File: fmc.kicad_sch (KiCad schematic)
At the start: 2 parts, among them P1 ASP-134604-01, P2 ASP-134604-01

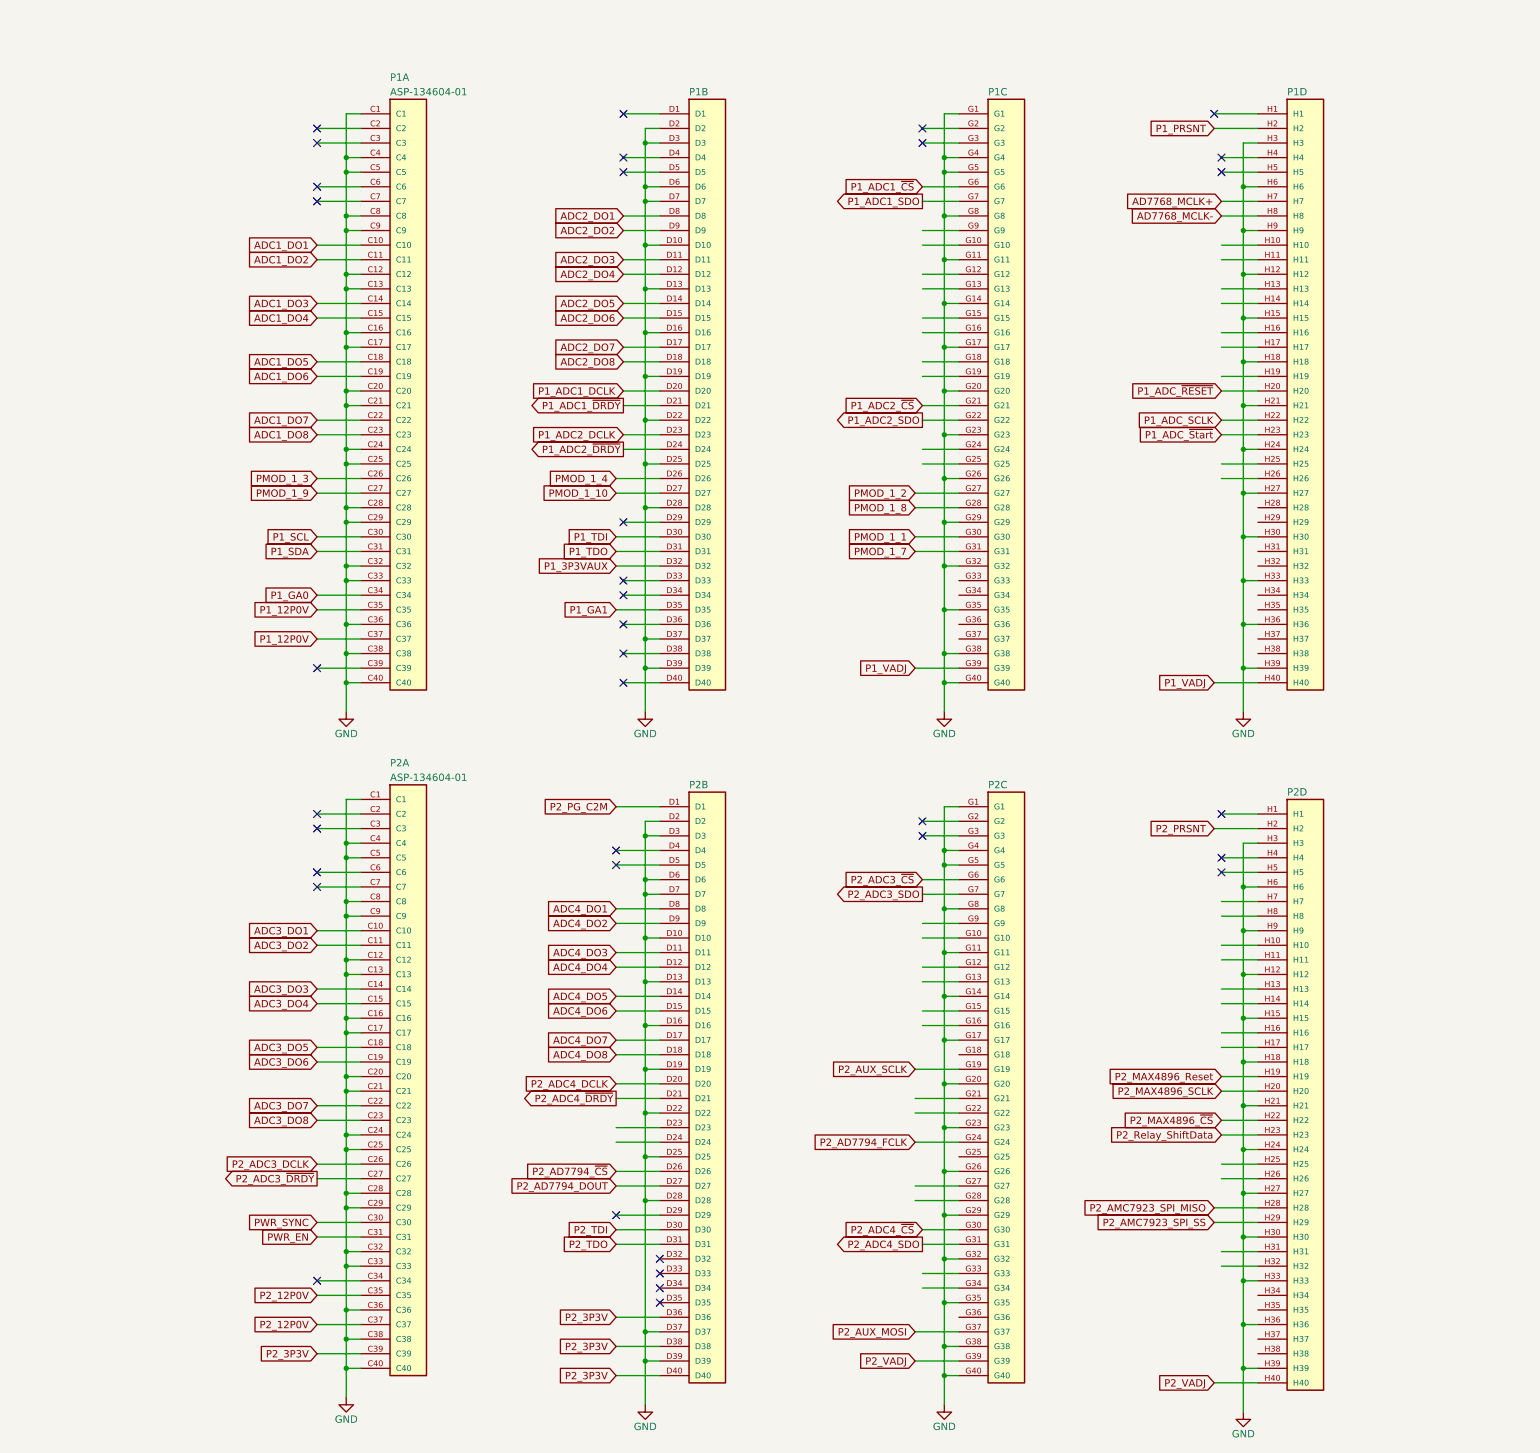
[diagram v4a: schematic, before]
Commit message: Schmatic Updates
Updated:
ADC MCLK signal
Removed PMOD connectors
Added Coax input for iRIG signal with 5V buffer
Moved around FMC pin mapping
Changed relay driver chip daisy chain order
Changed all input AFE to new design based around the INA851 chip
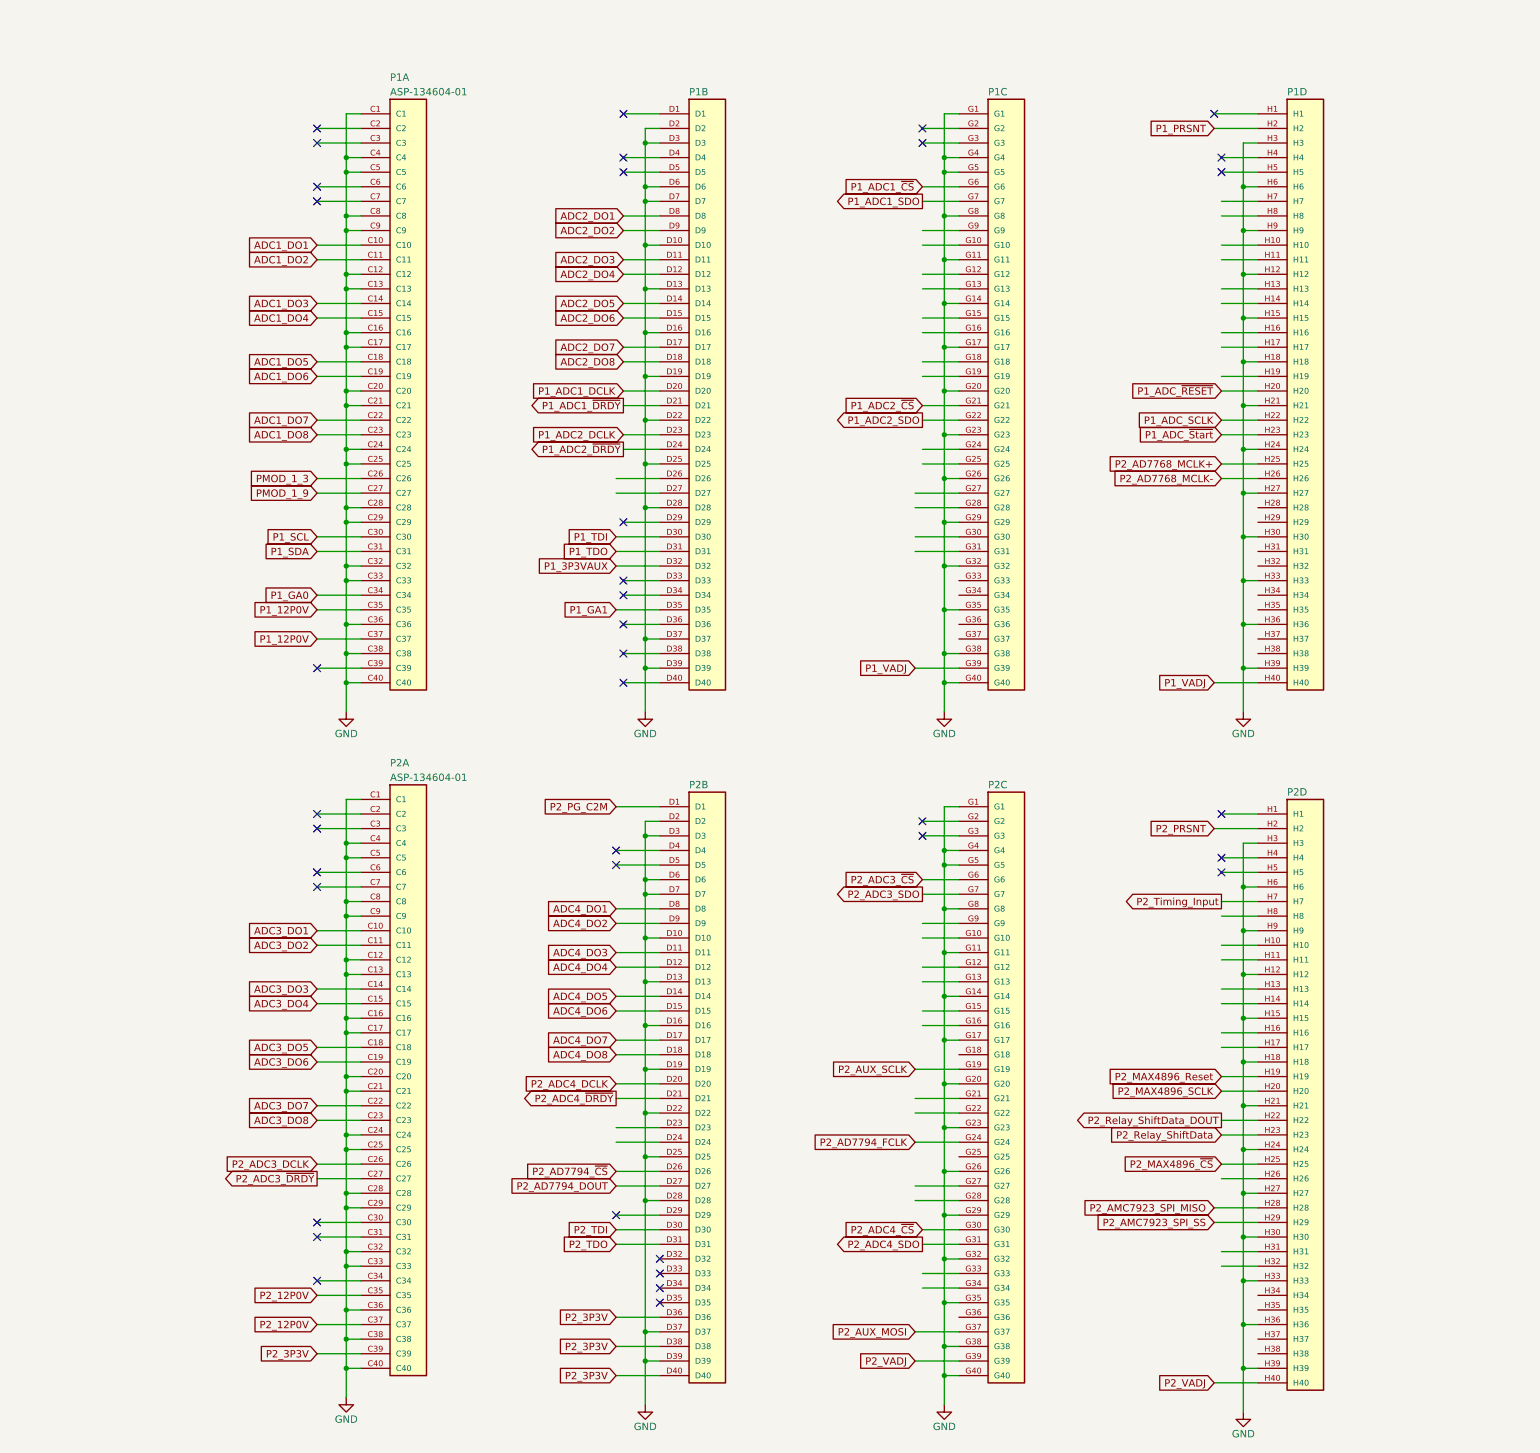
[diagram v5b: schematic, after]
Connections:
- net P2_MAX4896_~{CS}: now also P2.H25; no longer P2.H22
- net P2_Timing_Input: now reaches P2.H7
- net P2_AD7768_MCLK+: now reaches P1.H25
- net P2_AD7768_MCLK-: now reaches P1.H26
- net AD7768_MCLK+: no longer names the net of P1.H7
- net AD7768_MCLK-: no longer names the net of P1.H8
- net PMOD_1_1: no longer names the net of P1.G30
- net PMOD_1_10: no longer names the net of P1.D27
- net PMOD_1_2: no longer names the net of P1.G27
- net PMOD_1_4: no longer names the net of P1.D26
- net PMOD_1_7: no longer names the net of P1.G31
- net PMOD_1_8: no longer names the net of P1.G28
- net PWR_EN: no longer names the net of P2.C31
- net PWR_SYNC: no longer names the net of P2.C30
- new net P2_Relay_ShiftData_DOUT: P2.H22
- no-connect marks 36 -> 38
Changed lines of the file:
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@@
   (no_connect (at 171.45 41.91))
   (no_connect (at 177.8 233.68))
+  (no_connect (at 118.11 224.79))
   (no_connect (at 274.32 31.75))
   (no_connect (at 171.45 125.73))
@@
   (no_connect (at 223.52 36.83))
   (no_connect (at 171.45 102.87))
+  (no_connect (at 118.11 227.33))
   (no_connect (at 171.45 39.37))
   (no_connect (at 170.18 162.56))
@@
     )
   )
-  (global_label "AD7768_MCLK-" (shape input) (at 275.59 49.53 180) (fields_autoplaced)
-    (effects (font (size 1.27 1.27)) (justify right))
-    (property "Intersheetrefs" "${INTERSHEET_REFS}" (at 257.8487 49.53 0)
-      (effects (font (size 1.27 1.27)) (justify right) hide)
-    )
-  )
-  (global_label "PMOD_1_1" (shape input) (at 222.25 105.41 180) (fields_autoplaced)
-    (effects (font (size 1.27 1.27)) (justify right))
-    (property "Intersheetrefs" "${INTERSHEET_REFS}" (at 209.6681 105.41 0)
-      (effects (font (size 1.27 1.27)) (justify right) hide)
-    )
-  )
   (global_label "ADC1_DO5" (shape input) (at 118.11 74.93 180) (fields_autoplaced)
     (effects (font (size 1.27 1.27)) (justify right))
@@
     )
   )
+  (global_label "P2_MAX4896_~{CS}" (shape input) (at 275.59 214.63 180) (fields_autoplaced)
+    (effects (font (size 1.27 1.27)) (justify right))
+    (property "Intersheetrefs" "${INTERSHEET_REFS}" (at 257.1231 214.63 0)
+      (effects (font (size 1.27 1.27)) (justify right) hide)
+    )
+  )
   (global_label "P2_ADC4_~{DRDY}" (shape output) (at 170.18 203.2 180) (fields_autoplaced)
     (effects (font (size 1.27 1.27)) (justify right))
@@
     )
   )
-  (global_label "AD7768_MCLK+" (shape input) (at 275.59 46.99 180) (fields_autoplaced)
-    (effects (font (size 1.27 1.27)) (justify right))
-    (property "Intersheetrefs" "${INTERSHEET_REFS}" (at 257.8487 46.99 0)
-      (effects (font (size 1.27 1.27)) (justify right) hide)
-    )
-  )
   (global_label "P1_VADJ" (shape input) (at 222.25 128.27 180) (fields_autoplaced)
     (effects (font (size 1.27 1.27)) (justify right))
@@
     )
   )
+  (global_label "P2_Relay_ShiftData_DOUT" (shape output) (at 275.59 207.01 180) (fields_autoplaced)
+    (effects (font (size 1.27 1.27)) (justify right))
+    (property "Intersheetrefs" "${INTERSHEET_REFS}" (at 248.4751 207.01 0)
+      (effects (font (size 1.27 1.27)) (justify right) hide)
+    )
+  )
   (global_label "P1_ADC_~{Start}" (shape input) (at 275.59 87.63 180) (fields_autoplaced)
     (effects (font (size 1.27 1.27)) (justify right))
@@
     )
   )
+  (global_label "P2_Timing_Input" (shape output) (at 275.59 168.91 180) (fields_autoplaced)
+    (effects (font (size 1.27 1.27)) (justify right))
+    (property "Intersheetrefs" "${INTERSHEET_REFS}" (at 257.2441 168.91 0)
+      (effects (font (size 1.27 1.27)) (justify right) hide)
+    )
+  )
   (global_label "ADC1_DO4" (shape input) (at 118.11 67.31 180) (fields_autoplaced)
     (effects (font (size 1.27 1.27)) (justify right))
@@
     )
   )
-  (global_label "PMOD_1_8" (shape input) (at 222.25 100.33 180) (fields_autoplaced)
-    (effects (font (size 1.27 1.27)) (justify right))
-    (property "Intersheetrefs" "${INTERSHEET_REFS}" (at 209.6681 100.33 0)
-      (effects (font (size 1.27 1.27)) (justify right) hide)
-    )
-  )
   (global_label "P2_ADC3_~{CS}" (shape input) (at 223.52 165.1 180) (fields_autoplaced)
     (effects (font (size 1.27 1.27)) (justify right))
@@
     )
   )
-  (global_label "P2_MAX4896_~{CS}" (shape input) (at 275.59 207.01 180) (fields_autoplaced)
-    (effects (font (size 1.27 1.27)) (justify right))
-    (property "Intersheetrefs" "${INTERSHEET_REFS}" (at 257.1231 207.01 0)
-      (effects (font (size 1.27 1.27)) (justify right) hide)
-    )
-  )
   (global_label "ADC4_DO7" (shape input) (at 170.18 193.04 180) (fields_autoplaced)
     (effects (font (size 1.27 1.27)) (justify right))
@@
     )
   )
-  (global_label "PWR_EN" (shape input) (at 118.11 227.33 180) (fields_autoplaced)
-    (effects (font (size 1.27 1.27)) (justify right))
-    (property "Intersheetrefs" "${INTERSHEET_REFS}" (at 107.6863 227.33 0)
-      (effects (font (size 1.27 1.27)) (justify right) hide)
-    )
-  )
   (global_label "P2_PRSNT" (shape input) (at 274.32 156.21 180) (fields_autoplaced)
     (effects (font (size 1.27 1.27)) (justify right))
@@
     )
   )
+  (global_label "P2_AD7768_MCLK-" (shape input) (at 275.59 95.25 180) (fields_autoplaced)
+    (effects (font (size 1.27 1.27)) (justify right))
+    (property "Intersheetrefs" "${INTERSHEET_REFS}" (at 254.4016 95.25 0)
+      (effects (font (size 1.27 1.27)) (justify right) hide)
+    )
+  )
   (global_label "P1_ADC1_~{DRDY}" (shape output) (at 171.45 82.55 180) (fields_autoplaced)
     (effects (font (size 1.27 1.27)) (justify right))
@@
     )
   )
-  (global_label "PMOD_1_10" (shape input) (at 170.18 97.79 180) (fields_autoplaced)
-    (effects (font (size 1.27 1.27)) (justify right))
-    (property "Intersheetrefs" "${INTERSHEET_REFS}" (at 156.3886 97.79 0)
-      (effects (font (size 1.27 1.27)) (justify right) hide)
-    )
-  )
   (global_label "P1_ADC1_SDO" (shape output) (at 223.52 46.99 180) (fields_autoplaced)
     (effects (font (size 1.27 1.27)) (justify right))
@@
     )
   )
-  (global_label "PMOD_1_4" (shape input) (at 170.18 95.25 180) (fields_autoplaced)
-    (effects (font (size 1.27 1.27)) (justify right))
-    (property "Intersheetrefs" "${INTERSHEET_REFS}" (at 157.5981 95.25 0)
-      (effects (font (size 1.27 1.27)) (justify right) hide)
-    )
-  )
   (global_label "P1_12P0V" (shape input) (at 118.11 118.11 180) (fields_autoplaced)
     (effects (font (size 1.27 1.27)) (justify right))
@@
     )
   )
-  (global_label "PMOD_1_7" (shape input) (at 222.25 107.95 180) (fields_autoplaced)
-    (effects (font (size 1.27 1.27)) (justify right))
-    (property "Intersheetrefs" "${INTERSHEET_REFS}" (at 209.6681 107.95 0)
-      (effects (font (size 1.27 1.27)) (justify right) hide)
-    )
-  )
   (global_label "P2_12P0V" (shape input) (at 118.11 237.49 180) (fields_autoplaced)
     (effects (font (size 1.27 1.27)) (justify right))
@@
     )
   )
-  (global_label "PWR_SYNC" (shape input) (at 118.11 224.79 180) (fields_autoplaced)
-    (effects (font (size 1.27 1.27)) (justify right))
-    (property "Intersheetrefs" "${INTERSHEET_REFS}" (at 105.2672 224.79 0)
-      (effects (font (size 1.27 1.27)) (justify right) hide)
-    )
-  )
   (global_label "P1_PRSNT" (shape input) (at 274.32 34.29 180) (fields_autoplaced)
     (effects (font (size 1.27 1.27)) (justify right))
@@
     )
   )
+  (global_label "P2_AD7768_MCLK+" (shape input) (at 275.59 92.71 180) (fields_autoplaced)
+    (effects (font (size 1.27 1.27)) (justify right))
+    (property "Intersheetrefs" "${INTERSHEET_REFS}" (at 254.4016 92.71 0)
+      (effects (font (size 1.27 1.27)) (justify right) hide)
+    )
+  )
   (global_label "ADC3_DO8" (shape input) (at 118.11 207.01 180) (fields_autoplaced)
     (effects (font (size 1.27 1.27)) (justify right))
@@
       (effects (font (size 1.27 1.27)) (justify right) hide)
     )
-  )
-  (global_label "PMOD_1_2" (shape input) (at 222.25 97.79 180) (fields_autoplaced)
-    (effects (font (size 1.27 1.27)) (justify right))
-    (property "Intersheetrefs" "${INTERSHEET_REFS}" (at 209.6681 97.79 0)
-      (effects (font (size 1.27 1.27)) (justify right) hide)
-    )
